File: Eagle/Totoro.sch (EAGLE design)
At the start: 62 parts, among them IC1 MCP6004, J1 AUDIO_JACK_3.5MMDCI, T1 BC546A

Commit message: hw-v010
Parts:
- BAL, CUT, O1FRQ, O1FRQ1, O1FRQ2, O1FRQ3: value 100k(B) -> 10k; device SparkFun-Resistors:POTENTIOMETER-PTH-9MM-1/20W-20%-KIT -> SparkFun-Resistors:POTENTIOMETER-GATE-SWAPPED
- OLVL: value 100k(A) -> 10k; device SparkFun-Resistors:POTENTIOMETER-PTH-9MM-1/20W-20%-KIT -> SparkFun-Resistors:POTENTIOMETER-GATE-SWAPPED
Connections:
- removed net N$30: M3.1, O1FRQ1.A, O1FRQ1.S, O1FRQ2.A, O1FRQ2.S, O1FRQ3.A, O1FRQ3.S
- net N$31: now also M3.1, O1FRQ1.A, O1FRQ1.S, O1FRQ2.A, O1FRQ2.S, O1FRQ3.A, O1FRQ3.S
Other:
- moved on the sheet: C3, M5, M6, R8

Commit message: v100 added with minor fixes and ontop batteries
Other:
- note added: "Latest design files: https://github.com/Atarity/totoro-synth"
- note added: "V1.0.0 (2023-08-08)"
- moved on the sheet: BATT1, BATT2, GND, LED1, POW, R20, V+, V-

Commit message: version 101
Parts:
- renumbered O1FRQ to O2FRQ
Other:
- note added: "Latest design files: github.com/Atarity/totoro-synth"
- note added: "Original schematic: syntherjack.net/totoro-1-ic-simple-synth/"
- note added: "V1.0.1 (2023-12-01)"
- note removed: "Latest design files: https://github.com/Atarity/totoro-synth"
- note removed: "Original schematics: https://syntherjack.net/totoro-1-ic-simple-synth/"
- note removed: "V1.0.0 (2023-08-08)"

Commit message: 100k pot fix
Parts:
- BAL, CUT, O1FRQ1, O1FRQ2, O1FRQ3, O2FRQ: value 10k -> 100k(B)
- OLVL: value 10k -> 100k(A)
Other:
- note added: "MOD points: - M1-2 - generator "sync" - M3-4 - keyboard expander - M4 - OSC1 output - M5-6 - OSC1 range - M7 - OSC2 output - M8-9 - filter input - M10 - filter CV input"
- note added: "V1.0.1 (2023-12-18)"
- note removed: "V1.0.1 (2023-12-01)"
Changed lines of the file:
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@@
 </classes>
 <parts>
-<part name="O2FRQ" library="SparkFun-Resistors" deviceset="POTENTIOMETER" device="-GATE-SWAPPED" value="10k"/>
-<part name="BAL" library="SparkFun-Resistors" deviceset="POTENTIOMETER" device="-GATE-SWAPPED" value="10k"/>
+<part name="O2FRQ" library="SparkFun-Resistors" deviceset="POTENTIOMETER" device="-GATE-SWAPPED" value="100k(B)"/>
+<part name="BAL" library="SparkFun-Resistors" deviceset="POTENTIOMETER" device="-GATE-SWAPPED" value="100k(B)"/>
 <part name="R1" library="SparkFun-Resistors" deviceset="RESISTOR" device="AXIAL-0.3" value="1k"/>
 <part name="R2" library="SparkFun-Resistors" deviceset="RESISTOR" device="AXIAL-0.3" value="100k"/>
@@
 <part name="SUPPLY8" library="supply2" library_urn="urn:adsk.eagle:library:372" deviceset="GND" device=""/>
 <part name="R19" library="SparkFun-Resistors" deviceset="RESISTOR" device="AXIAL-0.3" value="10k"/>
-<part name="CUT" library="SparkFun-Resistors" deviceset="POTENTIOMETER" device="-GATE-SWAPPED" value="10k"/>
+<part name="CUT" library="SparkFun-Resistors" deviceset="POTENTIOMETER" device="-GATE-SWAPPED" value="100k(B)"/>
 <part name="M10" library="SparkFun-Connectors" deviceset="CONN_01" device=""/>
 <part name="C7" library="SparkFun-Capacitors" deviceset="10UF-POLAR" device="-RADIAL-2.5MM-25V-20%" value="1uF"/>
-<part name="OLVL" library="SparkFun-Resistors" deviceset="POTENTIOMETER" device="-GATE-SWAPPED" value="10k"/>
+<part name="OLVL" library="SparkFun-Resistors" deviceset="POTENTIOMETER" device="-GATE-SWAPPED" value="100k(A)"/>
 <part name="SUPPLY10" library="supply2" library_urn="urn:adsk.eagle:library:372" deviceset="GND" device=""/>
 <part name="J1" library="SparkFun-Connectors" deviceset="AUDIO_JACK_3.5MM" device="DCI" value="AUDIO_JACK_3.5MMDCI"/>
-<part name="O1FRQ1" library="SparkFun-Resistors" deviceset="POTENTIOMETER" device="-GATE-SWAPPED" value="10k"/>
+<part name="O1FRQ1" library="SparkFun-Resistors" deviceset="POTENTIOMETER" device="-GATE-SWAPPED" value="100k(B)"/>
 <part name="R10" library="SparkFun-Resistors" deviceset="RESISTOR" device="AXIAL-0.3" value="10k"/>
 <part name="G1" library="SparkFun-Switches" deviceset="MECHANICAL-KEYBOARD" device="1U"/>
-<part name="O1FRQ2" library="SparkFun-Resistors" deviceset="POTENTIOMETER" device="-GATE-SWAPPED" value="10k"/>
+<part name="O1FRQ2" library="SparkFun-Resistors" deviceset="POTENTIOMETER" device="-GATE-SWAPPED" value="100k(B)"/>
 <part name="R11" library="SparkFun-Resistors" deviceset="RESISTOR" device="AXIAL-0.3" value="10k"/>
 <part name="G2" library="SparkFun-Switches" deviceset="MECHANICAL-KEYBOARD" device="1U"/>
 <part name="G3" library="SparkFun-Switches" deviceset="MECHANICAL-KEYBOARD" device="1U"/>
 <part name="R12" library="SparkFun-Resistors" deviceset="RESISTOR" device="AXIAL-0.3" value="10k"/>
-<part name="O1FRQ3" library="SparkFun-Resistors" deviceset="POTENTIOMETER" device="-GATE-SWAPPED" value="10k"/>
+<part name="O1FRQ3" library="SparkFun-Resistors" deviceset="POTENTIOMETER" device="-GATE-SWAPPED" value="100k(B)"/>
 <part name="M3" library="SparkFun-Connectors" deviceset="CONN_01" device=""/>
 <part name="M4" library="SparkFun-Connectors" deviceset="CONN_01" device=""/>
@@
 <text x="212.598" y="7.366" size="5.08" layer="97" font="vector" ratio="4">POWER</text>
 <text x="-7.62" y="175.26" size="5.08" layer="97">Latest design files:  github.com/Atarity/totoro-synth</text>
-<text x="320.04" y="-95.504" size="3.81" layer="94" font="vector" ratio="10">V1.0.1 (2023-12-01)</text>
+<text x="320.04" y="-95.504" size="3.81" layer="94" font="vector" ratio="10">V1.0.1 (2023-12-18)</text>
+<text x="146.558" y="-45.974" size="2.54" layer="97" font="vector" ratio="4">MOD points:
+- M1-2 - generator "sync"
+- M3-4 - keyboard expander
+- M4 - OSC1 output
+- M5-6 - OSC1 range
+- M7 - OSC2 output
+- M8-9 - filter input
+- M10 - filter CV input</text>
 </plain>
 <instances>
 <instance part="O2FRQ" gate="G$1" x="7.62" y="66.04" smashed="yes">
-<attribute name="NAME" x="-1.778" y="66.294" size="1.778" layer="95" font="vector"/>
+<attribute name="NAME" x="-1.524" y="66.802" size="1.778" layer="95" font="vector"/>
+<attribute name="VALUE" x="1.524" y="65.532" size="1.778" layer="95" font="vector" rot="R180" align="bottom-center"/>
 </instance>
 <instance part="BAL" gate="G$1" x="241.3" y="66.04" smashed="yes" rot="MR180">
-<attribute name="NAME" x="244.348" y="66.294" size="1.778" layer="95" font="vector" rot="MR90"/>
+<attribute name="NAME" x="238.506" y="66.548" size="1.778" layer="95" font="vector" rot="MR0"/>
+<attribute name="VALUE" x="235.712" y="65.786" size="1.778" layer="95" font="vector" rot="MR180" align="bottom-center"/>
 </instance>
 <instance part="R1" gate="G$1" x="7.62" y="48.26" smashed="yes" rot="R90">
@@
 </instance>
 <instance part="CUT" gate="G$1" x="325.12" y="109.22" smashed="yes" rot="MR0">
-<attribute name="NAME" x="322.072" y="108.966" size="1.778" layer="95" font="vector" rot="MR270"/>
+<attribute name="NAME" x="328.168" y="111.506" size="1.778" layer="95" font="vector" rot="MR180"/>
+<attribute name="VALUE" x="330.962" y="106.934" size="1.778" layer="95" font="vector" rot="MR0" align="bottom-center"/>
 </instance>
 <instance part="M10" gate="G$1" x="312.42" y="96.52" smashed="yes" rot="R180">
@@
 </instance>
 <instance part="OLVL" gate="G$1" x="337.82" y="35.56" smashed="yes">
-<attribute name="NAME" x="335.026" y="37.592" size="1.778" layer="95" font="vector" rot="R180"/>
+<attribute name="NAME" x="329.692" y="35.814" size="1.778" layer="95" font="vector"/>
+<attribute name="VALUE" x="331.978" y="35.052" size="1.778" layer="95" font="vector" rot="R180" align="bottom-center"/>
 </instance>
 <instance part="SUPPLY10" gate="GND" x="337.82" y="17.78" smashed="yes">
@@
 </instance>
 <instance part="O1FRQ1" gate="G$1" x="60.96" y="-48.26" smashed="yes" rot="MR180">
-<attribute name="NAME" x="51.054" y="-48.768" size="1.778" layer="95" font="vector" rot="MR180"/>
+<attribute name="NAME" x="58.166" y="-47.752" size="1.778" layer="95" font="vector" rot="MR0"/>
+<attribute name="VALUE" x="53.848" y="-48.768" size="1.778" layer="95" font="vector" rot="MR180" align="bottom-center"/>
 </instance>
 <instance part="R10" gate="G$1" x="60.96" y="-63.5" smashed="yes" rot="R270">
@@
 </instance>
 <instance part="O1FRQ2" gate="G$1" x="81.28" y="-48.26" smashed="yes" rot="MR180">
-<attribute name="NAME" x="71.374" y="-48.768" size="1.778" layer="95" font="vector" rot="MR180"/>
+<attribute name="NAME" x="79.248" y="-47.752" size="1.778" layer="95" font="vector" rot="MR0"/>
+<attribute name="VALUE" x="75.184" y="-48.768" size="1.778" layer="95" font="vector" rot="MR180" align="bottom-center"/>
 </instance>
 <instance part="R11" gate="G$1" x="81.28" y="-63.5" smashed="yes" rot="R270">
@@
 </instance>
 <instance part="O1FRQ3" gate="G$1" x="99.06" y="-48.26" smashed="yes" rot="MR180">
-<attribute name="NAME" x="89.154" y="-48.768" size="1.778" layer="95" font="vector" rot="MR180"/>
+<attribute name="NAME" x="98.044" y="-47.752" size="1.778" layer="95" font="vector" rot="MR0"/>
+<attribute name="VALUE" x="93.726" y="-48.514" size="1.778" layer="95" font="vector" rot="MR180" align="bottom-center"/>
 </instance>
 <instance part="M3" gate="G$1" x="40.64" y="-38.1" smashed="yes">
@@
 </drawing>
 <compatibility>
+<note version="6.3" minversion="6.2.2" severity="warning">
+Since Version 6.2.2 text objects can contain more than one line,
+which will not be processed correctly with this version.
+</note>
 <note version="8.2" severity="warning">
 Since Version 8.2, EAGLE supports online libraries. The ids

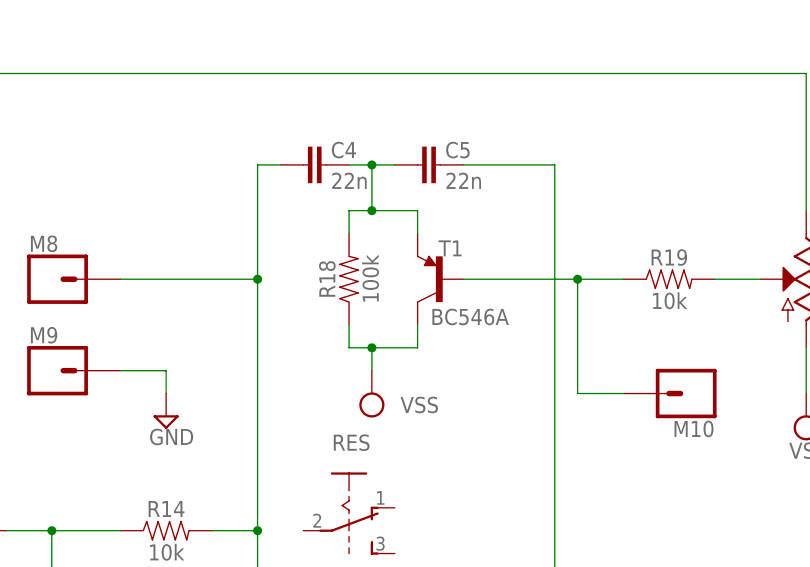
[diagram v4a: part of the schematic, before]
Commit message: Transistor symbol fix
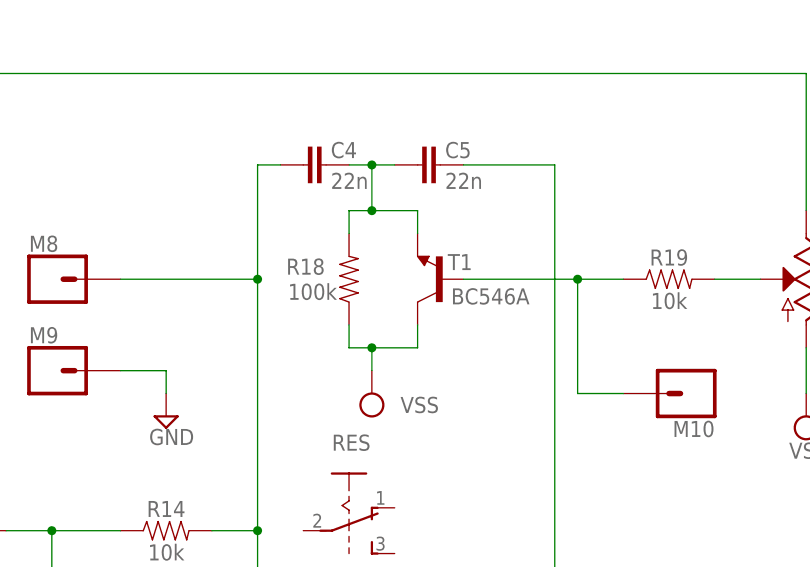
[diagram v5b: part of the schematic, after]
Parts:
- T1: device User-Submitted:TRANSISTOR_PNPBC558 -> transistor-npn:BC546A
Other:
- moved on the sheet: T1
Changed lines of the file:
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@@
 <part name="C5" library="rcl" library_urn="urn:adsk.eagle:library:334" deviceset="C-EU" device="050-024X044" package3d_urn="urn:adsk.eagle:package:23643/1" value="22n"/>
 <part name="C4" library="rcl" library_urn="urn:adsk.eagle:library:334" deviceset="C-EU" device="050-024X044" package3d_urn="urn:adsk.eagle:package:23643/1" value="22n"/>
-<part name="T1" library="User-Submitted" deviceset="TRANSISTOR_PNP" device="BC558" value="BC546A"/>
 <part name="SUPPLY8" library="supply2" library_urn="urn:adsk.eagle:library:372" deviceset="GND" device=""/>
 <part name="R19" library="SparkFun-Resistors" deviceset="RESISTOR" device="AXIAL-0.3" value="10k"/>
@@
 <part name="SUPPLY7" library="supply2" library_urn="urn:adsk.eagle:library:372" deviceset="GND" device=""/>
 <part name="FRAME1" library="frames" library_urn="urn:adsk.eagle:library:229" deviceset="DINA3_L" device=""/>
+<part name="T1" library="transistor-npn" library_urn="urn:adsk.eagle:library:398" deviceset="BC546*" device="" package3d_urn="urn:adsk.eagle:package:28989/2" technology="A"/>
 </parts>
 <sheets>
@@
 </instance>
 <instance part="R18" gate="G$1" x="274.32" y="109.22" smashed="yes" rot="R90">
-<attribute name="NAME" x="272.796" y="109.22" size="1.778" layer="95" font="vector" rot="R90" align="bottom-center"/>
-<attribute name="VALUE" x="275.844" y="109.22" size="1.778" layer="96" font="vector" rot="R90" align="top-center"/>
+<attribute name="NAME" x="269.494" y="111.506" size="1.778" layer="95" font="vector" rot="R180" align="bottom-center"/>
+<attribute name="VALUE" x="270.256" y="106.934" size="1.778" layer="96" font="vector" rot="R180" align="top-center"/>
 </instance>
 <instance part="R16" gate="G$1" x="254" y="48.26" smashed="yes">
@@
 <attribute name="NAME" x="272.288" y="122.682" size="1.778" layer="95"/>
 <attribute name="VALUE" x="272.288" y="119.253" size="1.778" layer="96"/>
-</instance>
-<instance part="T1" gate="G$1" x="284.48" y="109.22" smashed="yes" rot="MR0">
-<attribute name="NAME" x="287.02" y="111.76" size="1.778" layer="95" rot="MR0"/>
-<attribute name="VALUE" x="292.1" y="104.14" size="1.778" layer="96" rot="MR0"/>
 </instance>
 <instance part="SUPPLY8" gate="GND" x="266.7" y="35.56" smashed="yes">
@@
 <attribute name="SHEET" x="365.76" y="-110.49" size="2.54" layer="94"/>
 <attribute name="DRAWING_NAME" x="297.18" y="-95.25" size="5.08" layer="94" font="vector" ratio="10"/>
+</instance>
+<instance part="T1" gate="G$1" x="284.48" y="109.22" smashed="yes" rot="R180">
+<attribute name="NAME" x="288.036" y="112.014" size="1.778" layer="95" rot="R180"/>
+<attribute name="VALUE" x="294.386" y="108.204" size="1.778" layer="96" rot="R180"/>
 </instance>
 </instances>
@@
 <wire x1="274.32" y1="114.3" x2="274.32" y2="116.84" width="0.1524" layer="91"/>
 <wire x1="274.32" y1="116.84" x2="276.86" y2="116.84" width="0.1524" layer="91"/>
-<pinref part="T1" gate="G$1" pin="E"/>
 <wire x1="276.86" y1="116.84" x2="281.94" y2="116.84" width="0.1524" layer="91"/>
 <wire x1="281.94" y1="116.84" x2="281.94" y2="114.3" width="0.1524" layer="91"/>
@@
 <junction x="276.86" y="121.92"/>
 <junction x="276.86" y="116.84"/>
+<pinref part="T1" gate="G$1" pin="E"/>
 </segment>
 </net>
@@
 <wire x1="274.32" y1="104.14" x2="274.32" y2="101.6" width="0.1524" layer="91"/>
 <wire x1="274.32" y1="101.6" x2="276.86" y2="101.6" width="0.1524" layer="91"/>
-<pinref part="T1" gate="G$1" pin="C"/>
 <wire x1="276.86" y1="101.6" x2="281.94" y2="101.6" width="0.1524" layer="91"/>
 <wire x1="281.94" y1="101.6" x2="281.94" y2="104.14" width="0.1524" layer="91"/>
@@
 <junction x="276.86" y="101.6"/>
 <pinref part="SUPPLY16" gate="G$1" pin="VSS"/>
+<pinref part="T1" gate="G$1" pin="C"/>
 </segment>
 <segment>
@@
 <net name="N$18" class="0">
 <segment>
-<pinref part="T1" gate="G$1" pin="B"/>
 <pinref part="R19" gate="G$1" pin="1"/>
 <wire x1="287.02" y1="109.22" x2="299.72" y2="109.22" width="0.1524" layer="91"/>
@@
 <wire x1="299.72" y1="96.52" x2="299.72" y2="109.22" width="0.1524" layer="91"/>
 <junction x="299.72" y="109.22"/>
-</segment>
-</net>
+<pinref part="T1" gate="G$1" pin="B"/>
+</segment>
+</net>
